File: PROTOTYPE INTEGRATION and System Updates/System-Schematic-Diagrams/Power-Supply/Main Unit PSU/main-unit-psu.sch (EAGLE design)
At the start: 14 parts, among them U1 BA033CC0FP-E2TO252-3_ROM, U2 BA033CC0FP-E2TO252-3_ROM, U3 L7805CV, U4 RAC03-12SKRAC03-K_RCP

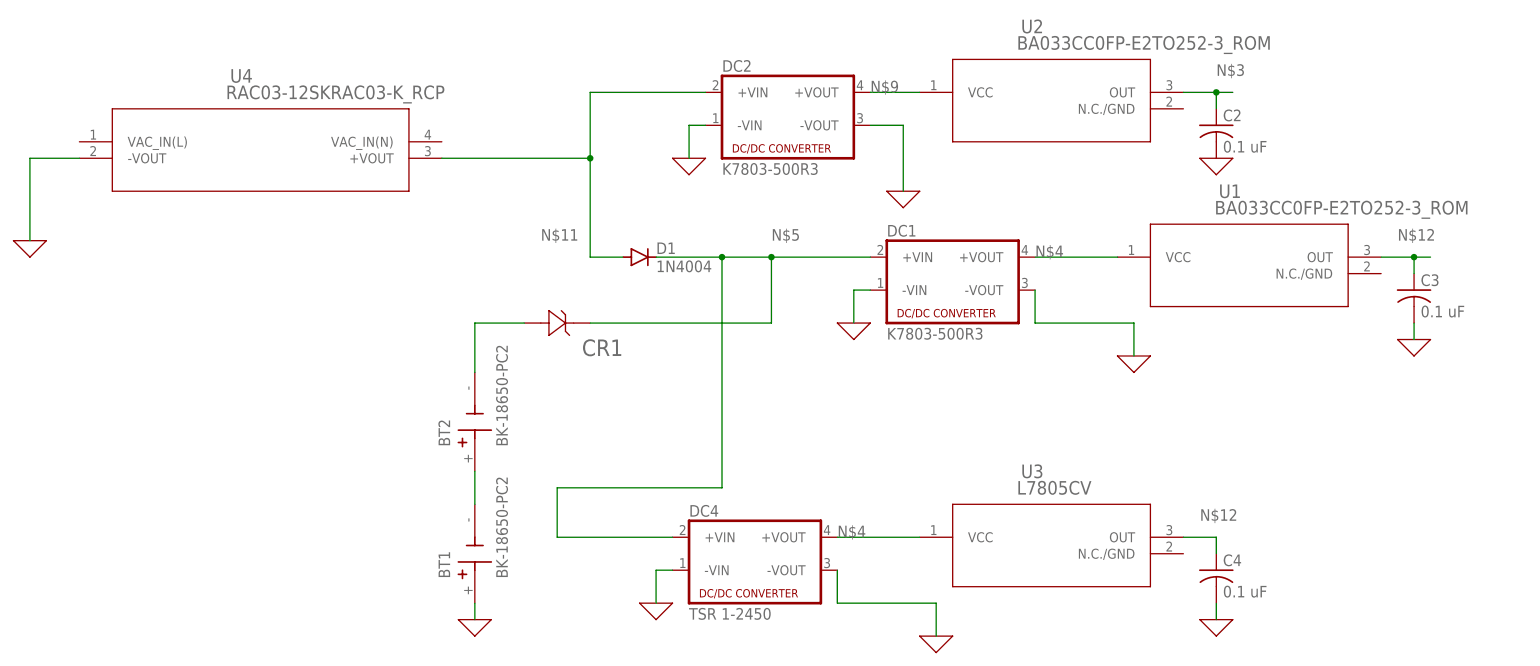
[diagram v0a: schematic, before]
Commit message: Updated Individual schematics, bd and pictures
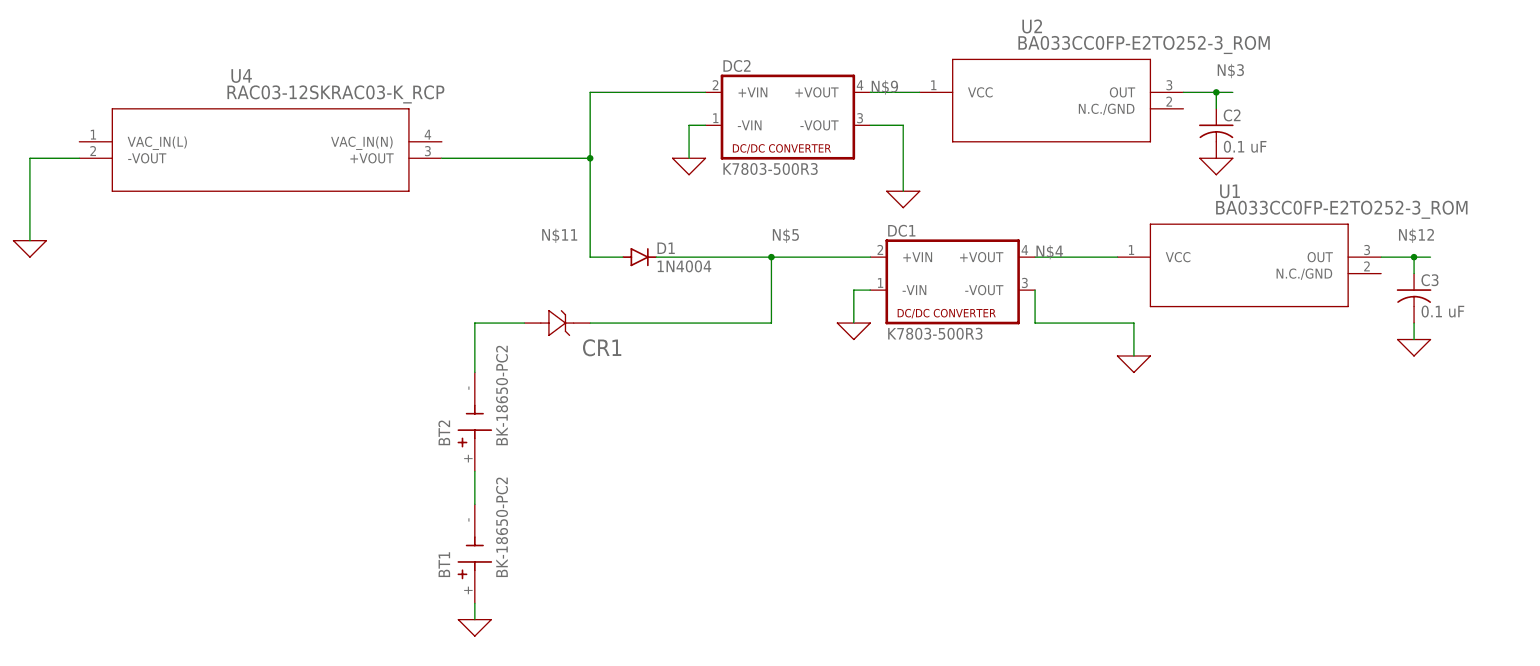
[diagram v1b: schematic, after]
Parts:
- removed C4: 0.1 uF, rcl:C-US050-024X044
- removed DC4: TSR 1-2450, dc-dc-converter:NME
- removed U3: L7805CV, 2023-03-08_12-17-23_Library:BA033CC0FP-E2TO252-3_ROM
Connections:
- net 0: no longer C4.2, DC4.-VIN, DC4.-VOUT
- net N$12: no longer C4.1, U3.OUT
- net N$4: no longer DC4.+VOUT, U3.VCC
- net N$5: no longer DC4.+VIN
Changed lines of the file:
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@@
 <part name="X_10" library="ngspice-simulation" library_urn="urn:adsk.eagle:library:527439" deviceset="GND" device=""/>
 <part name="X_11" library="ngspice-simulation" library_urn="urn:adsk.eagle:library:527439" deviceset="GND" device=""/>
-<part name="DC4" library="dc-dc-converter" library_urn="urn:adsk.eagle:library:208" deviceset="NME" device="" package3d_urn="urn:adsk.eagle:package:12313/1" value="TSR 1-2450"/>
-<part name="X_12" library="ngspice-simulation" library_urn="urn:adsk.eagle:library:527439" deviceset="GND" device=""/>
-<part name="U3" library="2023-03-08_12-17-23_Library" deviceset="BA033CC0FP-E2" device="TO252-3_ROM" value="L7805CV"/>
-<part name="X_13" library="ngspice-simulation" library_urn="urn:adsk.eagle:library:527439" deviceset="GND" device=""/>
-<part name="C4" library="rcl" library_urn="urn:adsk.eagle:library:334" deviceset="C-US" device="050-024X044" package3d_urn="urn:adsk.eagle:package:23643/1" value="0.1 uF"/>
-<part name="X_14" library="ngspice-simulation" library_urn="urn:adsk.eagle:library:527439" deviceset="GND" device=""/>
 <part name="U4" library="2023-04-05_11-47-46_Library" deviceset="RAC03-12SK" device="RAC03-K_RCP"/>
 <part name="X_1" library="ngspice-simulation" library_urn="urn:adsk.eagle:library:527439" deviceset="GND" device=""/>
@@
 <instance part="X_10" gate="G$1" x="195.58" y="43.18" smashed="yes"/>
 <instance part="X_11" gate="G$1" x="165.1" y="71.12" smashed="yes"/>
-<instance part="DC4" gate="G$1" x="93.98" y="10.16" smashed="yes">
-<attribute name="NAME" x="83.82" y="15.875" size="1.778" layer="95"/>
-<attribute name="VALUE" x="83.82" y="0" size="1.778" layer="96"/>
-</instance>
-<instance part="X_12" gate="G$1" x="78.74" y="2.54" smashed="yes"/>
-<instance part="U3" gate="A" x="116.84" y="12.7" smashed="yes">
-<attribute name="NAME" x="134.9746" y="21.8186" size="2.083" layer="95" ratio="6"/>
-<attribute name="VALUE" x="134.3352" y="19.2786" size="2.083" layer="96" ratio="6"/>
-</instance>
-<instance part="X_13" gate="G$1" x="121.92" y="-2.54" smashed="yes"/>
-<instance part="C4" gate="G$1" x="165.1" y="7.62" smashed="yes">
-<attribute name="NAME" x="166.116" y="8.255" size="1.778" layer="95"/>
-<attribute name="VALUE" x="166.116" y="3.429" size="1.778" layer="96"/>
-</instance>
-<instance part="X_14" gate="G$1" x="165.1" y="0" smashed="yes"/>
 <instance part="U4" gate="A" x="-12.7" y="73.66" smashed="yes">
 <attribute name="NAME" x="13.0546" y="82.7786" size="2.083" layer="95" ratio="6"/>
@@
 </segment>
 <segment>
-<pinref part="X_12" gate="G$1" pin="0"/>
-<pinref part="DC4" gate="G$1" pin="-VIN"/>
-<wire x1="78.74" y1="2.54" x2="78.74" y2="7.62" width="0.1524" layer="91"/>
-<wire x1="78.74" y1="7.62" x2="81.28" y2="7.62" width="0.1524" layer="91"/>
-</segment>
-<segment>
-<pinref part="DC4" gate="G$1" pin="-VOUT"/>
-<wire x1="106.68" y1="7.62" x2="106.68" y2="2.54" width="0.1524" layer="91"/>
-<wire x1="106.68" y1="2.54" x2="121.92" y2="2.54" width="0.1524" layer="91"/>
-<pinref part="X_13" gate="G$1" pin="0"/>
-<wire x1="121.92" y1="-2.54" x2="121.92" y2="2.54" width="0.1524" layer="91"/>
-</segment>
-<segment>
-<pinref part="X_14" gate="G$1" pin="0"/>
-<pinref part="C4" gate="G$1" pin="2"/>
-<wire x1="165.1" y1="0" x2="165.1" y2="2.54" width="0.1524" layer="91"/>
-</segment>
-<segment>
 <pinref part="X_1" gate="G$1" pin="0"/>
 <wire x1="-17.78" y1="58.42" x2="-17.78" y2="71.12" width="0.1524" layer="91"/>
@@
 <label x="137.16" y="55.88" size="1.778" layer="95"/>
 <pinref part="U1" gate="A" pin="VCC"/>
-</segment>
-<segment>
-<pinref part="DC4" gate="G$1" pin="+VOUT"/>
-<wire x1="106.68" y1="12.7" x2="119.38" y2="12.7" width="0.1524" layer="91"/>
-<label x="106.68" y="12.7" size="1.778" layer="95"/>
-<pinref part="U3" gate="A" pin="VCC"/>
 </segment>
 </net>
@@
 <junction x="195.58" y="55.88"/>
 </segment>
-<segment>
-<wire x1="160.02" y1="12.7" x2="165.1" y2="12.7" width="0.1524" layer="91"/>
-<label x="162.56" y="15.24" size="1.778" layer="95"/>
-<pinref part="U3" gate="A" pin="OUT"/>
-<pinref part="C4" gate="G$1" pin="1"/>
-<wire x1="165.1" y1="10.16" x2="165.1" y2="12.7" width="0.1524" layer="91"/>
-</segment>
 </net>
 <net name="N$6" class="0">
@@
 <net name="N$5" class="0">
 <segment>
-<pinref part="DC4" gate="G$1" pin="+VIN"/>
-<wire x1="63.5" y1="12.7" x2="81.28" y2="12.7" width="0.1524" layer="91"/>
-<wire x1="63.5" y1="12.7" x2="63.5" y2="20.32" width="0.1524" layer="91"/>
-<wire x1="63.5" y1="20.32" x2="88.9" y2="20.32" width="0.1524" layer="91"/>
 <pinref part="D1" gate="1" pin="C"/>
 <pinref part="DC1" gate="G$1" pin="+VIN"/>
-<wire x1="78.74" y1="55.88" x2="88.9" y2="55.88" width="0.1524" layer="91"/>
+<wire x1="78.74" y1="55.88" x2="96.52" y2="55.88" width="0.1524" layer="91"/>
 <label x="96.52" y="58.42" size="1.778" layer="95"/>
-<wire x1="88.9" y1="55.88" x2="96.52" y2="55.88" width="0.1524" layer="91"/>
 <wire x1="96.52" y1="55.88" x2="111.76" y2="55.88" width="0.1524" layer="91"/>
 <wire x1="68.58" y1="45.72" x2="96.52" y2="45.72" width="0.1524" layer="91"/>
 <wire x1="96.52" y1="45.72" x2="96.52" y2="55.88" width="0.1524" layer="91"/>
 <junction x="96.52" y="55.88"/>
-<wire x1="88.9" y1="20.32" x2="88.9" y2="55.88" width="0.1524" layer="91"/>
-<junction x="88.9" y="55.88"/>
 <pinref part="CR1" gate="A" pin="1"/>
 </segment>
